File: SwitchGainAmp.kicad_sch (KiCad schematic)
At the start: 16 parts, among them U12 4066, U8 LT1491CS

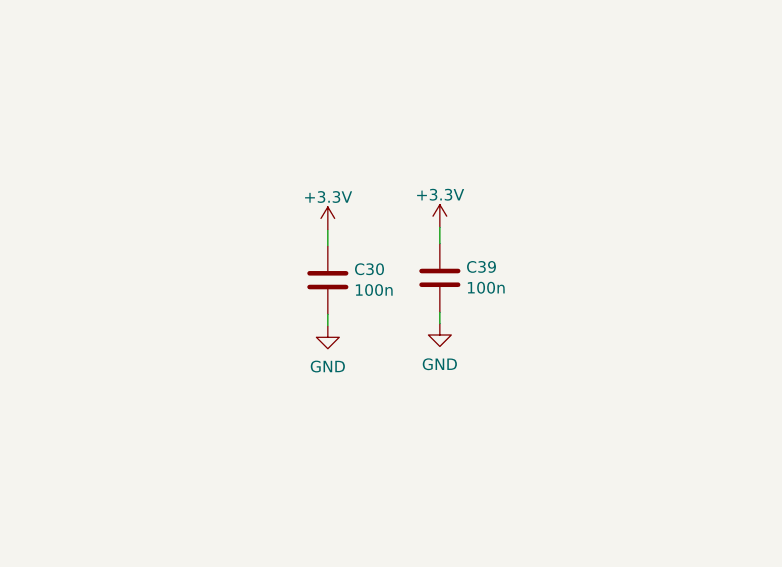
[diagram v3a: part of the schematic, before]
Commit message: had to push some symbols and lines to the grid for ERC clean
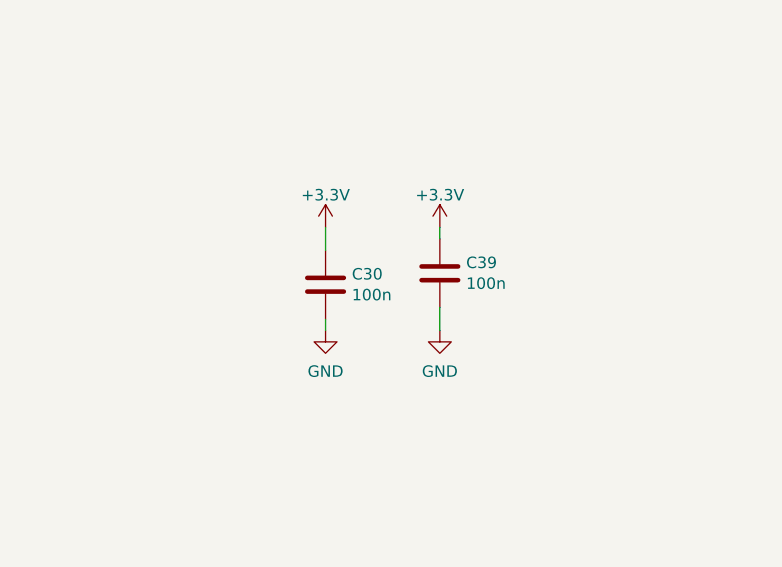
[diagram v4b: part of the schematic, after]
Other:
- moved on the sheet: C30, C39
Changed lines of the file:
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@@
     (stroke (width 0) (type default))
   )
-  (wire (pts (xy 256.794 139.192) (xy 256.794 140.462))
+  (wire (pts (xy 256.54 139.7) (xy 256.54 140.97))
     (stroke (width 0) (type default))
   )
@@
     (stroke (width 0) (type default))
   )
-  (wire (pts (xy 256.794 129.794) (xy 256.794 131.572))
-    (stroke (width 0) (type default))
-  )
-  (wire (pts (xy 269.24 129.54) (xy 269.24 131.318))
+  (wire (pts (xy 256.54 129.54) (xy 256.54 132.08))
+    (stroke (width 0) (type default))
+  )
+  (wire (pts (xy 269.24 129.54) (xy 269.24 130.81))
     (stroke (width 0) (type default))
   )
@@
     (stroke (width 0) (type default))
   )
-  (wire (pts (xy 269.24 138.938) (xy 269.24 140.208))
+  (wire (pts (xy 269.24 138.43) (xy 269.24 140.97))
     (stroke (width 0) (type default))
   )
@@
     )
   )
-  (symbol (lib_id "power:+3.3V") (at 256.794 129.794 0) (unit 1)
-    (in_bom yes) (on_board yes) (dnp no) (fields_autoplaced)
-    (property "Reference" "#PWR073" (at 256.794 133.604 0)
-      (effects (font (size 1.27 1.27)) hide)
-    )
-    (property "Value" "+3.3V" (at 256.794 126.1895 0)
-      (effects (font (size 1.27 1.27)))
-    )
-    (property "Footprint" "" (at 256.794 129.794 0)
-      (effects (font (size 1.27 1.27)) hide)
-    )
-    (property "Datasheet" "" (at 256.794 129.794 0)
+  (symbol (lib_id "power:+3.3V") (at 256.54 129.54 0) (unit 1)
+    (in_bom yes) (on_board yes) (dnp no) (fields_autoplaced)
+    (property "Reference" "#PWR073" (at 256.54 133.35 0)
+      (effects (font (size 1.27 1.27)) hide)
+    )
+    (property "Value" "+3.3V" (at 256.54 125.9355 0)
+      (effects (font (size 1.27 1.27)))
+    )
+    (property "Footprint" "" (at 256.54 129.54 0)
+      (effects (font (size 1.27 1.27)) hide)
+    )
+    (property "Datasheet" "" (at 256.54 129.54 0)
       (effects (font (size 1.27 1.27)) hide)
     )
@@
     )
   )
-  (symbol (lib_id "power:GND") (at 269.24 140.208 0) (unit 1)
-    (in_bom yes) (on_board yes) (dnp no) (fields_autoplaced)
-    (property "Reference" "#PWR071" (at 269.24 146.558 0)
-      (effects (font (size 1.27 1.27)) hide)
-    )
-    (property "Value" "GND" (at 269.24 144.7705 0)
-      (effects (font (size 1.27 1.27)))
-    )
-    (property "Footprint" "" (at 269.24 140.208 0)
-      (effects (font (size 1.27 1.27)) hide)
-    )
-    (property "Datasheet" "" (at 269.24 140.208 0)
+  (symbol (lib_id "power:GND") (at 269.24 140.97 0) (unit 1)
+    (in_bom yes) (on_board yes) (dnp no) (fields_autoplaced)
+    (property "Reference" "#PWR071" (at 269.24 147.32 0)
+      (effects (font (size 1.27 1.27)) hide)
+    )
+    (property "Value" "GND" (at 269.24 145.5325 0)
+      (effects (font (size 1.27 1.27)))
+    )
+    (property "Footprint" "" (at 269.24 140.97 0)
+      (effects (font (size 1.27 1.27)) hide)
+    )
+    (property "Datasheet" "" (at 269.24 140.97 0)
       (effects (font (size 1.27 1.27)) hide)
     )
@@
     )
   )
-  (symbol (lib_id "power:GND") (at 256.794 140.462 0) (unit 1)
-    (in_bom yes) (on_board yes) (dnp no) (fields_autoplaced)
-    (property "Reference" "#PWR074" (at 256.794 146.812 0)
-      (effects (font (size 1.27 1.27)) hide)
-    )
-    (property "Value" "GND" (at 256.794 145.0245 0)
-      (effects (font (size 1.27 1.27)))
-    )
-    (property "Footprint" "" (at 256.794 140.462 0)
-      (effects (font (size 1.27 1.27)) hide)
-    )
-    (property "Datasheet" "" (at 256.794 140.462 0)
+  (symbol (lib_id "power:GND") (at 256.54 140.97 0) (unit 1)
+    (in_bom yes) (on_board yes) (dnp no) (fields_autoplaced)
+    (property "Reference" "#PWR074" (at 256.54 147.32 0)
+      (effects (font (size 1.27 1.27)) hide)
+    )
+    (property "Value" "GND" (at 256.54 145.5325 0)
+      (effects (font (size 1.27 1.27)))
+    )
+    (property "Footprint" "" (at 256.54 140.97 0)
+      (effects (font (size 1.27 1.27)) hide)
+    )
+    (property "Datasheet" "" (at 256.54 140.97 0)
       (effects (font (size 1.27 1.27)) hide)
     )
@@
     )
   )
-  (symbol (lib_id "Device:C") (at 269.24 135.128 0) (unit 1)
-    (in_bom yes) (on_board yes) (dnp no)
-    (property "Reference" "C39" (at 272.161 133.9596 0)
+  (symbol (lib_id "Device:C") (at 269.24 134.62 0) (unit 1)
+    (in_bom yes) (on_board yes) (dnp no)
+    (property "Reference" "C39" (at 272.161 133.4516 0)
       (effects (font (size 1.27 1.27)) (justify left))
     )
-    (property "Value" "100n" (at 272.161 136.271 0)
+    (property "Value" "100n" (at 272.161 135.763 0)
       (effects (font (size 1.27 1.27)) (justify left))
     )
-    (property "Footprint" "Capacitor_SMD:C_0603_1608Metric" (at 270.2052 138.938 0)
-      (effects (font (size 1.27 1.27)) hide)
-    )
-    (property "Datasheet" "~" (at 269.24 135.128 0)
+    (property "Footprint" "Capacitor_SMD:C_0603_1608Metric" (at 270.2052 138.43 0)
+      (effects (font (size 1.27 1.27)) hide)
+    )
+    (property "Datasheet" "~" (at 269.24 134.62 0)
       (effects (font (size 1.27 1.27)) hide)
     )
@@
     )
   )
-  (symbol (lib_id "Device:C") (at 256.794 135.382 0) (unit 1)
-    (in_bom yes) (on_board yes) (dnp no)
-    (property "Reference" "C30" (at 259.715 134.2136 0)
+  (symbol (lib_id "Device:C") (at 256.54 135.89 0) (unit 1)
+    (in_bom yes) (on_board yes) (dnp no)
+    (property "Reference" "C30" (at 259.461 134.7216 0)
       (effects (font (size 1.27 1.27)) (justify left))
     )
-    (property "Value" "100n" (at 259.715 136.525 0)
+    (property "Value" "100n" (at 259.461 137.033 0)
       (effects (font (size 1.27 1.27)) (justify left))
     )
-    (property "Footprint" "Capacitor_SMD:C_0603_1608Metric" (at 257.7592 139.192 0)
-      (effects (font (size 1.27 1.27)) hide)
-    )
-    (property "Datasheet" "~" (at 256.794 135.382 0)
-      (effects (font (size 1.27 1.27)) hide)
-    )
+    (property "Footprint" "Capacitor_SMD:C_0603_1608Metric" (at 257.5052 139.7 0)
+      (effects (font (size 1.27 1.27)) hide)
+    )
+    (property "Datasheet" "~" (at 256.54 135.89 0)
+      (effects (font (size 1.27 1.27)) hide)
+    )
